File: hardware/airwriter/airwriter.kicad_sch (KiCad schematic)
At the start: 60 parts, among them J1 USB-C 5V in, J2 Mini-DIN-8 to printer, J3 Bring-up USB/UART, J4 Mini-DIN-8 LocalTalk, J6 I2C / Qwiic, SW1 BOOT bridge, SW2 MODE touch, U1 ESP32-S3-WROOM-1-N8R2, U2 MAX3490ESA+, U3 MAX3232ESE+, U4 AP7361C-33E, U5 USBLC6-2SC6, U6 SP3485EN-L, U7 PIC12F1840-I/P, U8 SP3485EN-L

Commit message: Rework schematic for the dot-panel face
Removes the MODE touch pad (SW2, R20, C19) and the two-LED WS2812 test
chain plus the logo-window trio (D1/C8, D2/C20, D4, D5, D6), killing
nets BTN_MODE, TOUCH_SENSE, LED_CHAIN, LOGO_CH1/2/3. D3's footprint
moves from the reverse-mount 1206 hole part to a plain top-side 0603
LED. LED_DATA on U1 pin 25 (IO48) is untouched.

Adds a 74AHCT1G125 single-gate buffer (U9, SOT-353) between LED_DATA
and a new LED_DATA5 net, decoupled with C29, so the 37-LED dot panel
(D10-D46, SK6812MINI-E, top-firing footprint) runs off a solid VBUS-
referenced signal rather than the ESP32's raw 3.3V GPIO. Each LED gets
its own 100nF decoupling cap (C30-C66); C21/C22 add 22uF of bulk VBUS
capacitance for the field. All LED power runs off VBUS (5V), not
+3V3 - the part's rated 3.7-5.5V.

Adds S1, an 8-position DIP bank wired to U1's internal pull-ups
(DIP1-8 on IO38/39/40/41/42/47/21/13), and SW3, a 6x6mm tact switch
on IO14 (BTN_TEST) reusing the pin TOUCH_SENSE vacated.

ERC is zero errors before and after (9 warnings baseline, all
pre-existing lib_symbol_mismatch noise; 79 after, adding one
lib_symbol_mismatch for U9 and 37 footprint_link_issues because the
brief's required top-firing SK6812MINI-E footprint has no stock KiCad
equivalent - only the ReverseMount variant ships - so Task 2 will need
to draw that footprint before layout). Netlist export confirms every
required node count: VBUS/LED_DATA/LED_DATA5/LED_CH01-36/DIP1-8/
BTN_TEST all correct, dead nets fully absent.

hardware/airwriter/tools_sch/ holds the surgery as reproducible
Python (a tiny embedded s-expression parser, the removal-set derivation
script, and the two apply scripts), plus the D1 SK6812MINI-E block
saved verbatim as the LED template before it was deleted.

Refs: W-573
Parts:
- removed C19, C20, C8: 100n, Capacitor_SMD:C_0603_1608Metric, symbol Device:C
- removed D1, D2: SK6812MINI-E, LED_SMD:LED_SK6812MINI-E_3.2x2.8mm_P1.5mm_ReverseMount, symbol LED:SK6812MINI-E
- removed D4, D5, D6: SK6812MINI, LED_SMD:LED_SK6812MINI_PLCC4_3.5x3.5mm_P1.75mm, symbol LED:SK6812MINI
- removed R20: 1k, Resistor_SMD:R_0603_1608Metric, symbol Device:R
- removed SW2: MODE touch, airwriter:TouchPad_Core_D9mm, symbol Switch:SW_Push
- added C21, C22: 22u, Capacitor_SMD:C_0805_2012Metric, symbol Device:C
- added C29, C30, C31, C32, C33, C34, C35, C36, C37, C38, C39, C40, C41, C42, C43, C44, C45, C46, C47, C48, C49, C50, C51, C52, C53, C54, C55, C56, C57, C58, C59, C60, C61, C62, C63, C64, C65, C66: 100n, Capacitor_SMD:C_0603_1608Metric, symbol Device:C
- added D10, D11, D12, D13, D14, D15, D16, D17, D18, D19, D20, D21, D22, D23, D24, D25, D26, D27, D28, D29, D30, D31, D32, D33, D34, D35, D36, D37, D38, D39, D40, D41, D42, D43, D44, D45, D46: SK6812MINI-E, LED_SMD:LED_SK6812MINI-E_3.2x2.8mm_P1.5mm, symbol LED:SK6812MINI-E
- added S1: DIP switch, 8-position, Button_Switch_THT:SW_DIP_SPSTx08_Slide_9.78x22.5mm_W7.62mm_P2.54mm, symbol Switch:SW_DIP_x08
- added SW3: TS-1002-BR16026, Button_Switch_THT:SW_PUSH_6mm_H13mm, symbol Switch:SW_Push
- added U9: 74AHCT1G125SE-7, Package_TO_SOT_SMD:SOT-353_SC-70-5, symbol 74xGxx:74AHCT1G125
- D3: footprint LED_SMD:LED_1206_3216Metric_ReverseMount_Hole1.8x2.4mm -> LED_SMD:LED_0603_1608Metric
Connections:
- net GND: now also C21.2, C22.2, C29.2, C30.2, C31.2, C32.2, C33.2, C34.2, C35.2, C36.2, C37.2, C38.2, C39.2, C40.2, C41.2, C42.2, C43.2, C44.2, C45.2, C46.2, C47.2, C48.2, C49.2, C50.2, C51.2, C52.2, C53.2, C54.2, C55.2, C56.2, C57.2, C58.2, C59.2, C60.2, C61.2, C62.2, C63.2, C64.2, C65.2, C66.2, D10.1 (VSS), D11.1 (VSS), D12.1 (VSS), D13.1 (VSS), D14.1 (VSS), D15.1 (VSS), D16.1 (VSS), D17.1 (VSS), D18.1 (VSS), D19.1 (VSS), D20.1 (VSS), D21.1 (VSS), D22.1 (VSS), D23.1 (VSS), D24.1 (VSS), D25.1 (VSS), D26.1 (VSS), D27.1 (VSS), D28.1 (VSS), D29.1 (VSS), D30.1 (VSS), D31.1 (VSS), D32.1 (VSS), D33.1 (VSS), D34.1 (VSS), D35.1 (VSS), D36.1 (VSS), D37.1 (VSS), D38.1 (VSS), D39.1 (VSS), D40.1 (VSS), D41.1 (VSS), D42.1 (VSS), D43.1 (VSS), D44.1 (VSS), D45.1 (VSS), D46.1 (VSS), S1.10, S1.11, S1.12, S1.13, S1.14, S1.15, S1.16, S1.9, SW3.2, U9.1, U9.3 (GND)
- net LED_DATA: now also U9.2
- net VBUS: now also C21.1, C22.1, C29.1, C30.1, C31.1, C32.1, C33.1, C34.1, C35.1, C36.1, C37.1, C38.1, C39.1, C40.1, C41.1, C42.1, C43.1, C44.1, C45.1, C46.1, C47.1, C48.1, C49.1, C50.1, C51.1, C52.1, C53.1, C54.1, C55.1, C56.1, C57.1, C58.1, C59.1, C60.1, C61.1, C62.1, C63.1, C64.1, C65.1, C66.1, D10.3 (VDD), D11.3 (VDD), D12.3 (VDD), D13.3 (VDD), D14.3 (VDD), D15.3 (VDD), D16.3 (VDD), D17.3 (VDD), D18.3 (VDD), D19.3 (VDD), D20.3 (VDD), D21.3 (VDD), D22.3 (VDD), D23.3 (VDD), D24.3 (VDD), D25.3 (VDD), D26.3 (VDD), D27.3 (VDD), D28.3 (VDD), D29.3 (VDD), D30.3 (VDD), D31.3 (VDD), D32.3 (VDD), D33.3 (VDD), D34.3 (VDD), D35.3 (VDD), D36.3 (VDD), D37.3 (VDD), D38.3 (VDD), D39.3 (VDD), D40.3 (VDD), D41.3 (VDD), D42.3 (VDD), D43.3 (VDD), D44.3 (VDD), D45.3 (VDD), D46.3 (VDD), U9.5 (VCC)
- net DIP8: now reaches U1.21 (IO13)
- net DIP8: now also S1.8
- net DIP7: now reaches U1.23 (IO21)
- net DIP7: now also S1.7
- net DIP6: now reaches U1.24 (IO47)
- net DIP6: now also S1.6
- net DIP1: now reaches U1.31 (IO38)
- net DIP1: now also S1.1
- net DIP2: now reaches U1.32 (IO39)
- net DIP2: now also S1.2
- net DIP3: now reaches U1.33 (IO40)
- net DIP3: now also S1.3
- net DIP4: now reaches U1.34 (IO41)
- net DIP4: now also S1.4
- net DIP5: now reaches U1.35 (IO42)
- net DIP5: now also S1.5
- net TOUCH_SENSE renamed BTN_TEST
- net BTN_TEST: now also SW3.1
- new net LED_CH01: D10.4 (DOUT), D11.2 (DIN)
- new net LED_CH02: D11.4 (DOUT), D12.2 (DIN)
- new net LED_CH03: D12.4 (DOUT), D13.2 (DIN)
- new net LED_CH04: D13.4 (DOUT), D14.2 (DIN)
- new net LED_CH05: D14.4 (DOUT), D15.2 (DIN)
- new net LED_CH06: D15.4 (DOUT), D16.2 (DIN)
- new net LED_CH07: D16.4 (DOUT), D17.2 (DIN)
- new net LED_CH08: D17.4 (DOUT), D18.2 (DIN)
- new net LED_CH09: D18.4 (DOUT), D19.2 (DIN)
- new net LED_CH10: D19.4 (DOUT), D20.2 (DIN)
- new net LED_CH11: D20.4 (DOUT), D21.2 (DIN)
- new net LED_CH12: D21.4 (DOUT), D22.2 (DIN)
- new net LED_CH13: D22.4 (DOUT), D23.2 (DIN)
- new net LED_CH14: D23.4 (DOUT), D24.2 (DIN)
- new net LED_CH15: D24.4 (DOUT), D25.2 (DIN)
- new net LED_CH16: D25.4 (DOUT), D26.2 (DIN)
- new net LED_CH17: D26.4 (DOUT), D27.2 (DIN)
- new net LED_CH18: D27.4 (DOUT), D28.2 (DIN)
- new net LED_CH19: D28.4 (DOUT), D29.2 (DIN)
- new net LED_CH20: D29.4 (DOUT), D30.2 (DIN)
- new net LED_CH21: D30.4 (DOUT), D31.2 (DIN)
- new net LED_CH22: D31.4 (DOUT), D32.2 (DIN)
- new net LED_CH23: D32.4 (DOUT), D33.2 (DIN)
- new net LED_CH24: D33.4 (DOUT), D34.2 (DIN)
- new net LED_CH25: D34.4 (DOUT), D35.2 (DIN)
- new net LED_CH26: D35.4 (DOUT), D36.2 (DIN)
- new net LED_CH27: D36.4 (DOUT), D37.2 (DIN)
- new net LED_CH28: D37.4 (DOUT), D38.2 (DIN)
- new net LED_CH29: D38.4 (DOUT), D39.2 (DIN)
- new net LED_CH30: D39.4 (DOUT), D40.2 (DIN)
- new net LED_CH31: D40.4 (DOUT), D41.2 (DIN)
- new net LED_CH32: D41.4 (DOUT), D42.2 (DIN)
- new net LED_CH33: D42.4 (DOUT), D43.2 (DIN)
- new net LED_CH34: D43.4 (DOUT), D44.2 (DIN)
- new net LED_CH35: D44.4 (DOUT), D45.2 (DIN)
- new net LED_CH36: D45.4 (DOUT), D46.2 (DIN)
- new net LED_DATA5: D10.2 (DIN), U9.4
- no-connect marks 31 -> 23

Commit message: Place the dot-panel board
Refs: W-573
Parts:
- D10, D11, D12, D13, D14, D15, D16, D17, D18, D19, D20, D21, D22, D23, D24, D25, D26, D27, D28, D29, D30, D31, D32, D33, D34, D35, D36, D37, D38, D39, D40, D41, D42, D43, D44, D45, D46: footprint LED_SMD:LED_SK6812MINI-E_3.2x2.8mm_P1.5mm -> airwriter:LED_SK6812MINI-E_3.2x2.8mm_P1.5mm_TopFiring

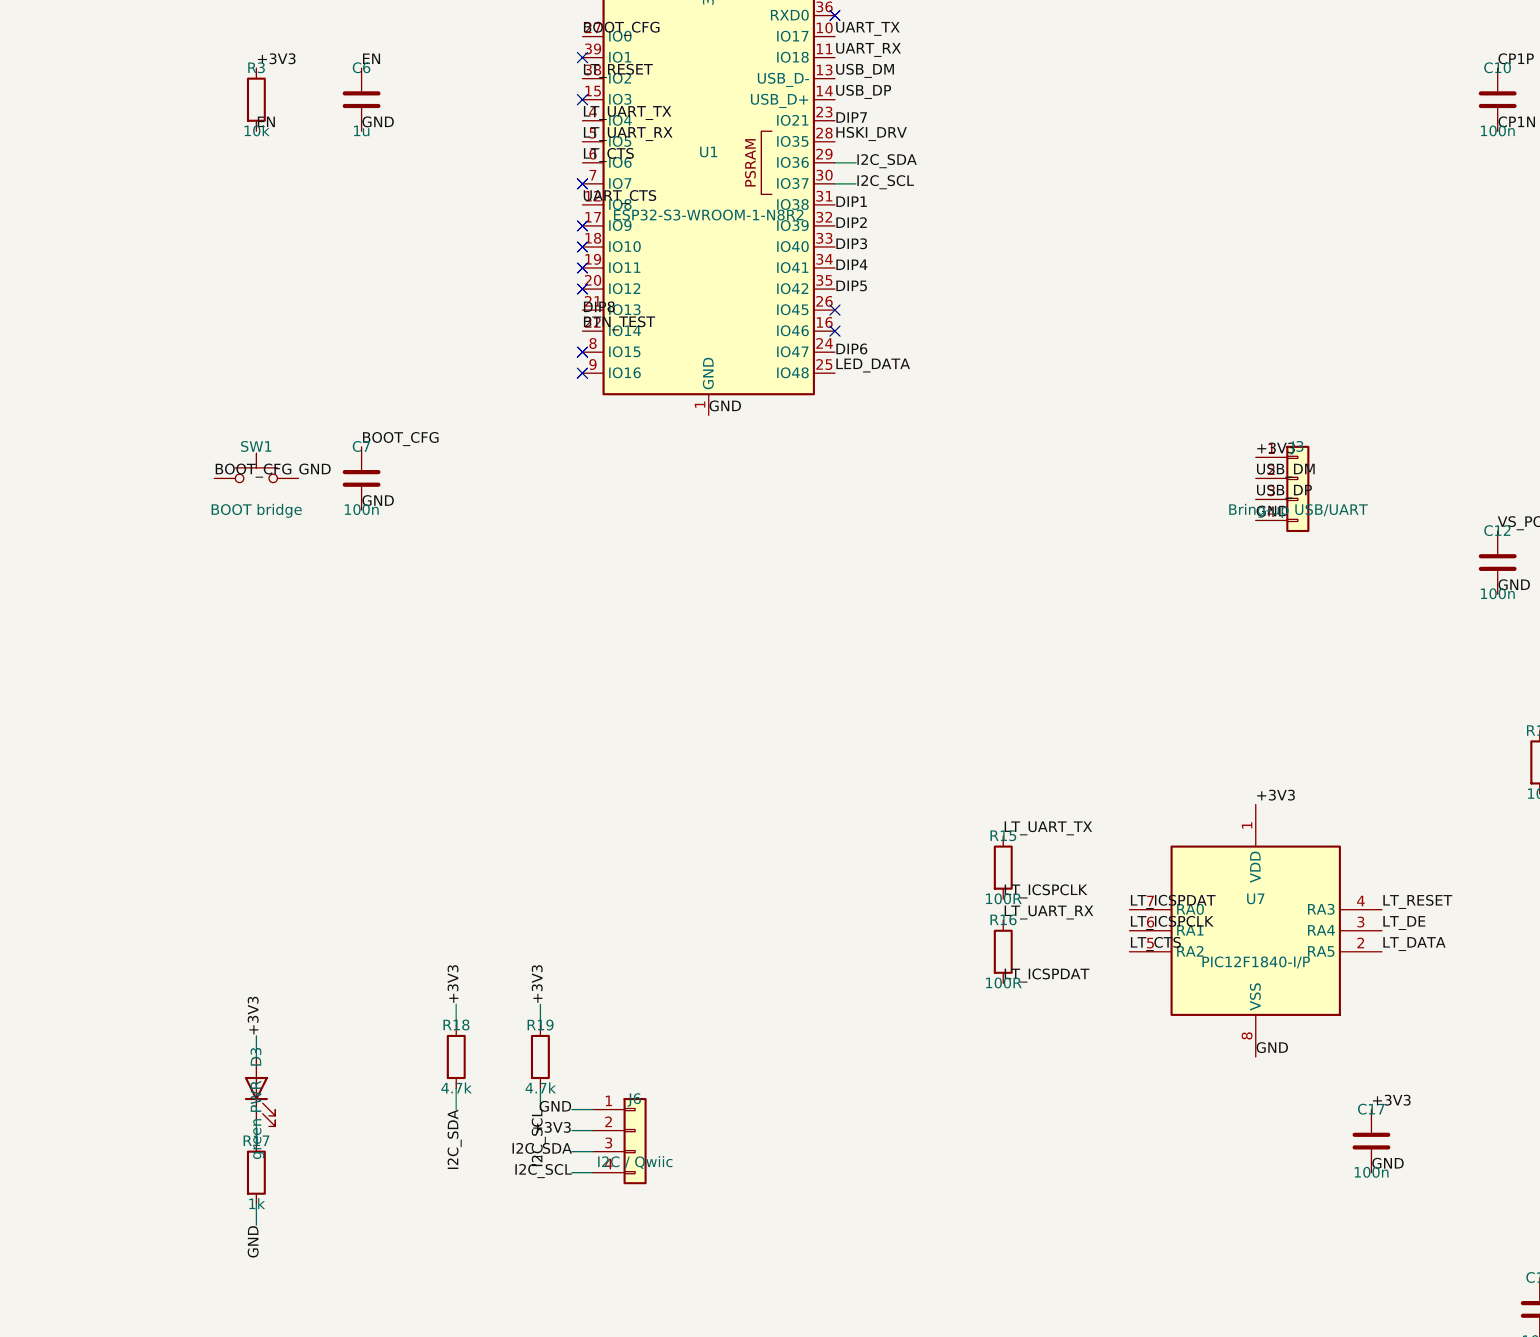
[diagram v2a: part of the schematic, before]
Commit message: Trim the fitted parts to the real feature set
Remove the I2C display header (J6) and its pull-ups (R18/R19) -- /I2C_SDA
and /I2C_SCL die entirely, IO36/IO37 go no-connect. Remove the USB pin
header (J3); /USB_DP and /USB_DM keep their other nodes (J1, U5, U1).
Swap SW1 from the tweezer-pad BootPads_Service footprint to a real
side-actuated SMD tact switch (Panasonic EVQP44B3M, LCSC C79164, in
stock) on the same /BOOT_CFG and /GND nets -- reset now works through a
case pinhole instead of bare pads. No stock KiCad footprint matches the
part, so lib/airwriter.pretty carries a derived one (pad geometry is a
conservative edge-mount estimate; Panasonic's outline drawing is
image-based, same gap class as the DP-08RP lookup earlier in this
project).

ERC: 0 errors. Board placement for the new/surviving parts is not final
here -- see the next commit.

Refs: W-573
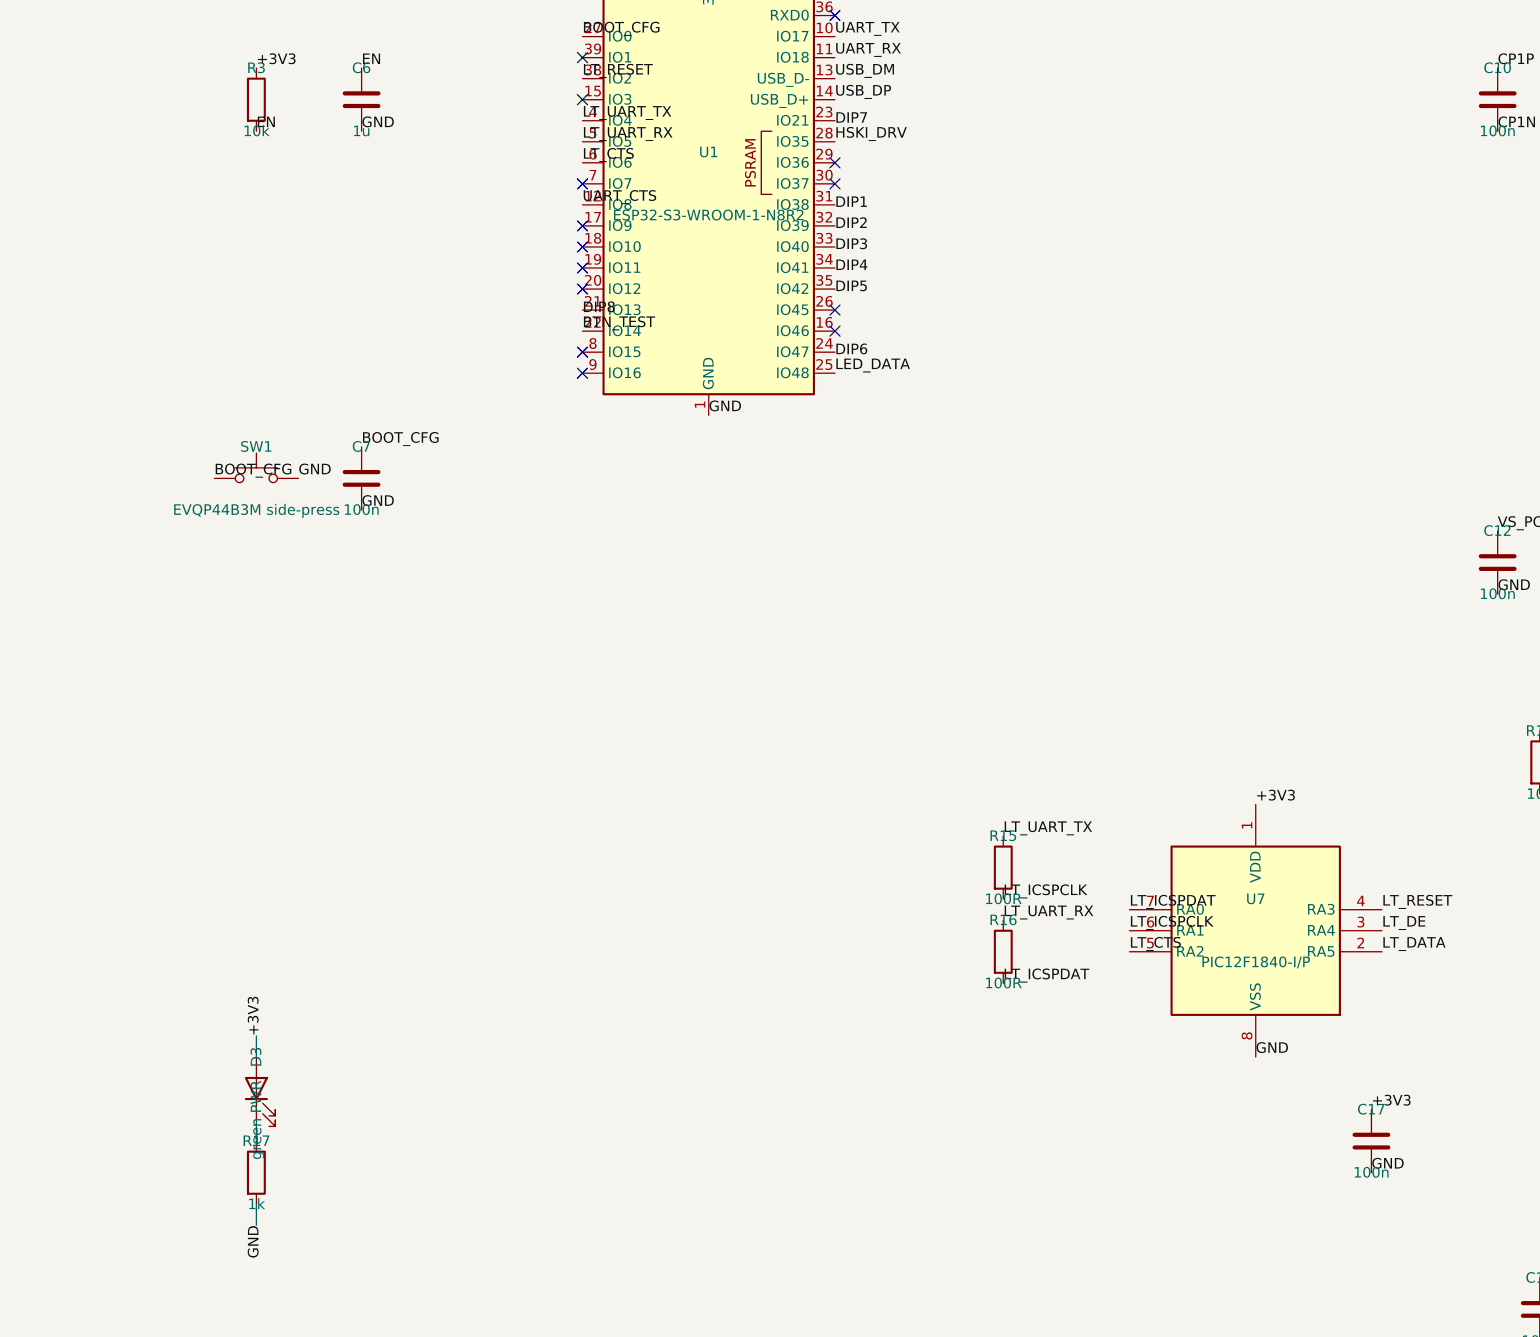
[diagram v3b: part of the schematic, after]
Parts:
- removed J3: Bring-up USB/UART, Connector_PinHeader_1.27mm:PinHeader_1x04_P1.27mm_Vertical, symbol Connector_Generic:Conn_01x04
- removed J6: I2C / Qwiic, Connector_JST:JST_SH_SM04B-SRSS-TB_1x04-1MP_P1.00mm_Horizontal, symbol Connector_Generic:Conn_01x04
- removed R18, R19: 4.7k, Resistor_SMD:R_0603_1608Metric, symbol Device:R
- SW1: value BOOT bridge -> EVQP44B3M side-press; footprint airwriter:BootPads_Service -> airwriter:EVQP44B3M_SidePress
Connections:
- net I2C_SCL: no longer names the net of U1.30 (IO37)
- net I2C_SDA: no longer names the net of U1.29 (IO36)
- no-connect marks 23 -> 25

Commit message: Give the edge controls their real bodies
S1 wore the stock top-slide DIP footprint, whose body, courtyard and 3D model
describe a different part. Built airwriter:SW_DIP_8_RightAngle_DP-08RP from the
manufacturer drawing, measured off the PDF's own vector paths rather than the
raster: the SVG was transformed to page coordinates and scaled by the drawing's
7.62mm pin-row dimension, giving 10.378 pt/mm.

That measurement corrected the brief. The body does NOT stand at the front pin
row -- it is centred on both rows, 0.994mm past each, for 9.61mm total. The
piano keys protrude 2.40mm past the body face, 1.30 wide, 0.90 thick, 0.40 below
the body top, aligned with the pin columns. Holes are 0.97 so the drill goes to
1.0mm, up from the stock 0.8mm.

S1 keeps its body face 0.2mm off the x=100 edge, exactly where it was, and the
keys now overhang 2.25mm past it -- which is how the mini-DINs already meet the
case, and what a side cutout needs to be pressable.

SW1 stays on EVQP44B3M. Its two candidate replacements share one KiCad footprint
whose courtyard is 7.80 x 5.50mm; turned to face west that needs 7.8mm of the
west edge and only 3.955mm exists between S1 and J2. The swap was never
geometrically possible, quite apart from EVQPUA02K being out of stock at LCSC and
EVQPUJ02K not being listed there. Recorded in the report: EVQPUC02K is the same
family, side-push, in stock, and shares a KiCad footprint with a STEP model, if
the west edge is ever rearranged to fit it.

Both parts now have 3D bodies -- hand-written VRML boxes at the measured
dimensions. SW1's had to be attached to the board instance too: a footprint
carries its own copy of the model reference from when it was placed, so adding
one to the library alone left it rendering bodiless.

U1 moves 0.6mm north. South of the module only 0.72mm of copper separated it
from J4, and seven signals leave that pad row westward; north of it 1.9mm sat
unused. Balanced at 1.32 and 1.01mm, both wide enough for two tracks. Without
i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
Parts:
- S1: footprint Button_Switch_THT:SW_DIP_SPSTx08_Slide_9.78x22.5mm_W7.62mm_P2.54mm -> airwriter:SW_DIP_8_RightAngle_DP-08RP

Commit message: Add LCSC part numbers to the schematic and BOM
Added an LCSC field to 51 schematic symbols (37 LEDs + 13 named parts)
and regenerated the BOM with an LCSC column alongside MPN.

Ref -> LCSC: D10-D46 C5149201 (SK6812MINI-E x37), U1 C2913204
(ESP32-S3-WROOM-1-N8R2), U2 C68934 (MAX3490ESA+T), U3 C15846
(MAX3232ESE+T), U4 C500795 (AP7361C-33E-13), U5 C7519 (USBLC6-2SC6),
U6/U8 C8963 (SP3485EN-L/TR), U9 C151417 (74AHCT1G125SE-7), J1 C165948
(TYPE-C-31-M-12), J2/J4 C5780060 (KMDGX-8S-BS), S1 C458097 (DP-08RP),
SW1 C79164 (EVQP44B3M), SW3 C920211 (TS-1002-BR16026).
Left blank (no clean LCSC part): U7 (PIC12F1840-I/P PDIP — LCSC stocks
only the SOIC), D3 (generic green 0603 LED), all generic R/C passives.

ERC unchanged (0 errors; the 42 lib_symbol_mismatch warnings are
pre-existing, identical pre/post edit). BOM still 30 grouped rows, LED
x37, DNP flags intact (R5, R6/R7, R9). Fab BOM + zip BOM regenerated.
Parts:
- D10, D11, D12, D13, D14, D15, D16, D17, D18, D19, D20, D21, D22, D23, D24, D25, D26, D27, D28, D29, D30, D31, D32, D33, D34, D35, D36, D37, D38, D39, D40, D41, D42, D43, D44, D45, D46: LCSC (none) -> C5149201
- J1: LCSC (none) -> C165948
- J2, J4: LCSC (none) -> C5780060
- S1: LCSC (none) -> C458097
- SW1: LCSC (none) -> C79164
- SW3: LCSC (none) -> C920211
- U1: LCSC (none) -> C2913204
- U2: LCSC (none) -> C68934
- U3: LCSC (none) -> C15846
- U4: LCSC (none) -> C500795
- U5: LCSC (none) -> C7519
- U6, U8: LCSC (none) -> C8963
- U9: LCSC (none) -> C151417

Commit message: Round 10 schematic: reset rewire, BOOT switch, LED series-R, U4 input cap, UART0 + test-point breakout
SW1 rewired IO0/BOOT -> EN so the case pinhole is a RESET (R3/C6 POR
intact, SW1 grounds EN). SW2 added = BOOT momentary switch, Omron
B3U-1000P (top-actuated SMD, LCSC C231329) on IO0<->GND near U1 --
EVQP44B3M side-press has no board-edge access near U1. R20 47R series on
/LED_DATA5 (U9.4 -> LED_DATA5R -> R20 -> LED_DATA5 -> D10). C67 1uF 0805
VBUS input cap at U4. UART0 broken out: U1 pin37=TXD0, pin36=RXD0.

The 8 board-only test points (VBUS, +3V3, GNDx2, EN, TXD0, RXD0,
LED_DATA5) are NOT schematic symbols (bare pads, not purchasable) and are
added directly in pcbnew -- see docs/round10-board-finishing.md.

ERC 0 errors (42 pre-existing lib_symbol_mismatch warnings). Board
sync/place/route is PENDING GUI work (dense hand-routed board needs
push-shove for the two long switch-rewire traces); board stays at HEAD.
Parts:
- added C67: 1u, Capacitor_SMD:C_0805_2012Metric, symbol Device:C
- added R20: 47R, Resistor_SMD:R_0603_1608Metric, symbol Device:R
- added SW2: B3U-1000P, Button_Switch_SMD:SW_SPST_B3U-1000P, symbol Switch:SW_Push
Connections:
- net BOOT_CFG: now also SW2.1; no longer SW1.1
- net EN: now also SW1.1
- net GND: now also C67.1, SW2.2
- net LED_DATA5: now also R20.1; no longer U9.4
- net VBUS: now also C67.2
- net RXD0: now reaches U1.36 (RXD0)
- net TXD0: now reaches U1.37 (TXD0)
- new net LED_DATA5R: R20.2, U9.4
- no-connect marks 25 -> 23
